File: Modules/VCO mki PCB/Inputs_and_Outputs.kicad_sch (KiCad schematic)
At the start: 9 parts, among them J1 Sync, J2 V/Oct, J3 Exp FM, J4 Lin FM, J5 PW Mod, J6 Senoid, J7 Triangle, J8 Square, J9 Sawtooth

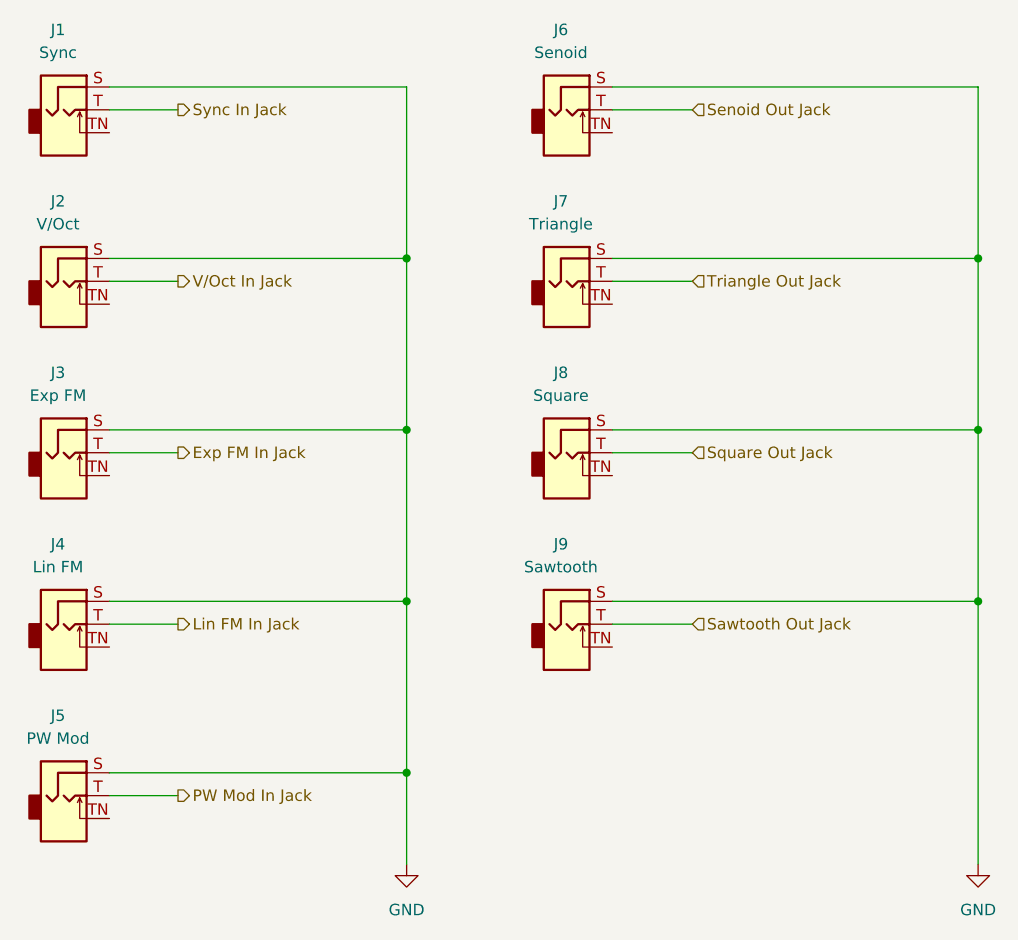
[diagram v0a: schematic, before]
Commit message: Designed VCO core and saw-to-tri circuits
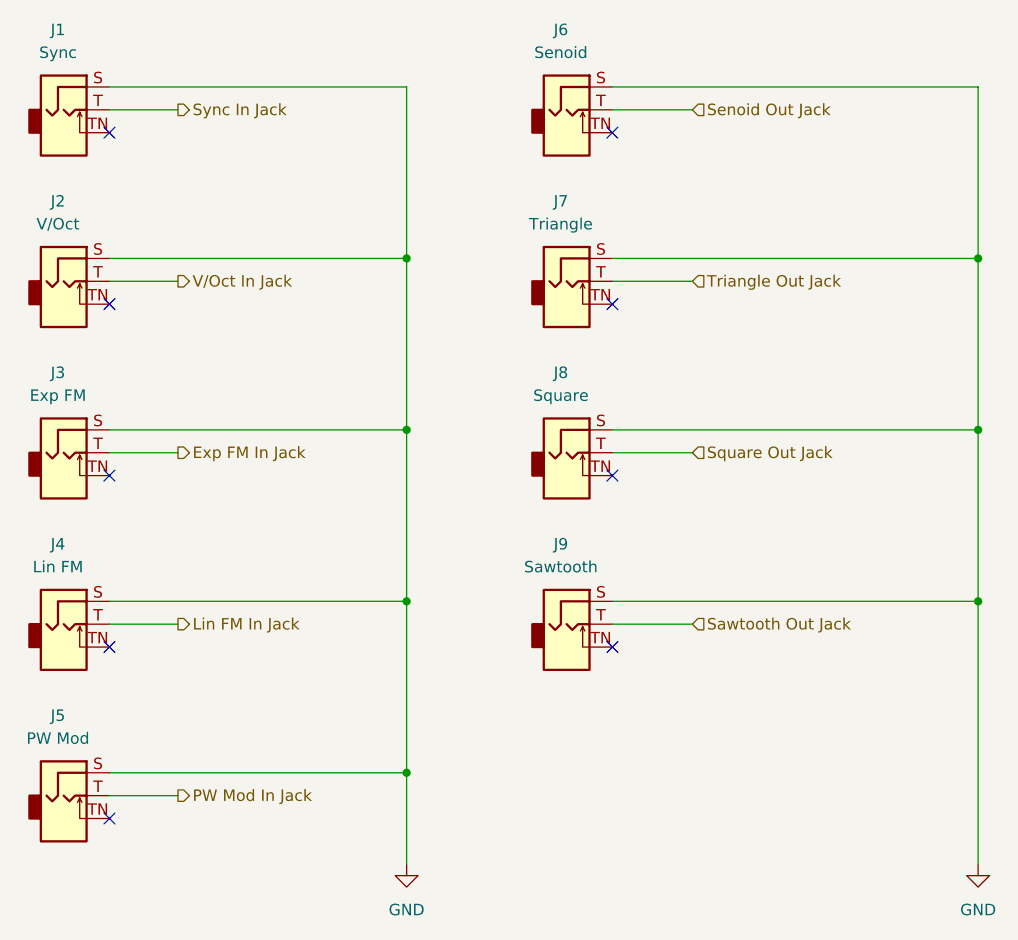
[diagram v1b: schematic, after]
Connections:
- no-connect marks 0 -> 9
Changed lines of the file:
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@@
 		(color 0 0 0 0)
+	)
+	(no_connect
+		(at 124.46 58.42)
+	)
+	(no_connect
+		(at 68.58 115.57)
+	)
+	(no_connect
+		(at 68.58 96.52)
+	)
+	(no_connect
+		(at 68.58 58.42)
+	)
+	(no_connect
+		(at 124.46 96.52)
+	)
+	(no_connect
+		(at 68.58 134.62)
+	)
+	(no_connect
+		(at 124.46 77.47)
+	)
+	(no_connect
+		(at 68.58 77.47)
+	)
+	(no_connect
+		(at 124.46 115.57)
 	)
 	(wire

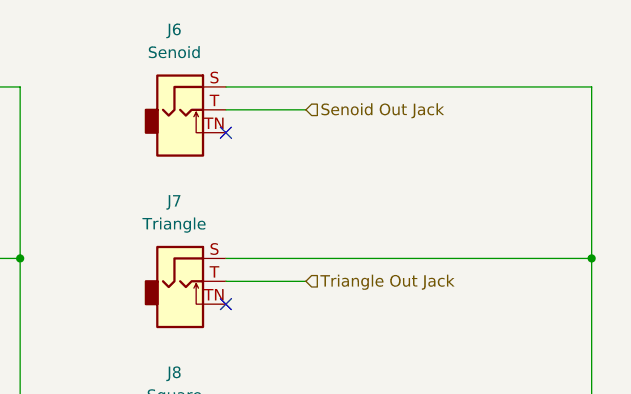
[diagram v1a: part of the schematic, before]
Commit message: Designed Sine Shaper circuit
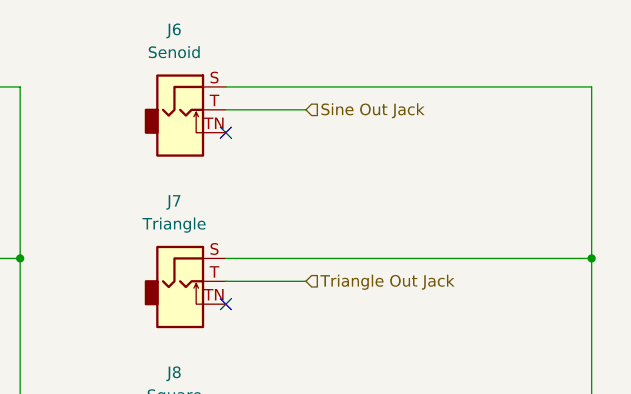
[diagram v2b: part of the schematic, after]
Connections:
- net Senoid Out Jack renamed Sine Out Jack
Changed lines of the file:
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@@
 		)
 	)
-	(hierarchical_label "Senoid Out Jack"
+	(hierarchical_label "Sine Out Jack"
 		(shape input)
 		(at 133.35 55.88 0)
